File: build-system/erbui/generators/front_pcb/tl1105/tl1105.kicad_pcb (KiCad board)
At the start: 2 copper layers, 1 part, among them SW1 SW_Push_Dual

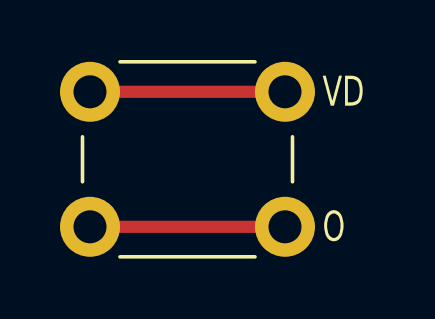
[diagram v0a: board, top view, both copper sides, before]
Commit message: Update erbui front pcb generator blocks labels to match boards conventions
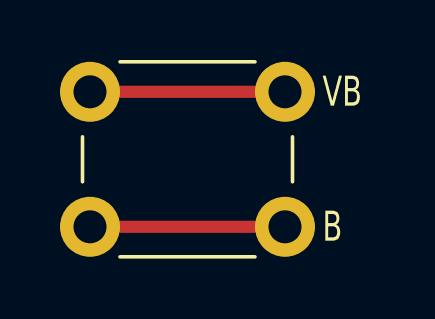
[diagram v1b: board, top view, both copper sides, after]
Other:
- board text added: "B"
- board text added: "VB"
- board text removed: "O"
- board text removed: "VD"
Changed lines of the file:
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@@
   )
   (setup
-    (last_trace_width 0.4064)
+    (last_trace_width 0.1524)
     (user_trace_width 0.1524)
     (user_trace_width 0.254)
@@
       (effects (font (size 1 1) (thickness 0.15)))
     )
+    (fp_line (start 3.25 -0.75) (end 6.25 -0.75) (layer F.Fab) (width 0.1))
+    (fp_line (start 6.25 -0.75) (end 6.25 5.25) (layer F.Fab) (width 0.1))
+    (fp_line (start 6.25 5.25) (end 0.25 5.25) (layer F.Fab) (width 0.1))
+    (fp_line (start 0.25 5.25) (end 0.25 -0.75) (layer F.Fab) (width 0.1))
+    (fp_line (start 0.25 -0.75) (end 3.25 -0.75) (layer F.Fab) (width 0.1))
+    (fp_line (start 7.75 6) (end 8 6) (layer F.CrtYd) (width 0.05))
+    (fp_line (start 8 6) (end 8 5.75) (layer F.CrtYd) (width 0.05))
+    (fp_line (start 7.75 -1.5) (end 8 -1.5) (layer F.CrtYd) (width 0.05))
+    (fp_line (start 8 -1.5) (end 8 -1.25) (layer F.CrtYd) (width 0.05))
+    (fp_line (start -1.5 -1.25) (end -1.5 -1.5) (layer F.CrtYd) (width 0.05))
+    (fp_line (start -1.5 -1.5) (end -1.25 -1.5) (layer F.CrtYd) (width 0.05))
+    (fp_line (start -1.5 5.75) (end -1.5 6) (layer F.CrtYd) (width 0.05))
+    (fp_line (start -1.5 6) (end -1.25 6) (layer F.CrtYd) (width 0.05))
+    (fp_line (start -1.25 -1.5) (end 7.75 -1.5) (layer F.CrtYd) (width 0.05))
+    (fp_line (start -1.5 5.75) (end -1.5 -1.25) (layer F.CrtYd) (width 0.05))
+    (fp_line (start 7.75 6) (end -1.25 6) (layer F.CrtYd) (width 0.05))
+    (fp_line (start 8 -1.25) (end 8 5.75) (layer F.CrtYd) (width 0.05))
+    (fp_line (start 1 5.5) (end 5.5 5.5) (layer F.SilkS) (width 0.12))
+    (fp_line (start -0.25 1.5) (end -0.25 3) (layer F.SilkS) (width 0.12))
+    (fp_line (start 5.5 -1) (end 1 -1) (layer F.SilkS) (width 0.12))
+    (fp_line (start 6.75 3) (end 6.75 1.5) (layer F.SilkS) (width 0.12))
     (fp_circle (center 3.25 2.25) (end 1.25 2.5) (layer F.Fab) (width 0.1))
-    (fp_line (start 6.75 3) (end 6.75 1.5) (layer F.SilkS) (width 0.12))
-    (fp_line (start 5.5 -1) (end 1 -1) (layer F.SilkS) (width 0.12))
-    (fp_line (start -0.25 1.5) (end -0.25 3) (layer F.SilkS) (width 0.12))
-    (fp_line (start 1 5.5) (end 5.5 5.5) (layer F.SilkS) (width 0.12))
-    (fp_line (start 8 -1.25) (end 8 5.75) (layer F.CrtYd) (width 0.05))
-    (fp_line (start 7.75 6) (end -1.25 6) (layer F.CrtYd) (width 0.05))
-    (fp_line (start -1.5 5.75) (end -1.5 -1.25) (layer F.CrtYd) (width 0.05))
-    (fp_line (start -1.25 -1.5) (end 7.75 -1.5) (layer F.CrtYd) (width 0.05))
-    (fp_line (start -1.5 6) (end -1.25 6) (layer F.CrtYd) (width 0.05))
-    (fp_line (start -1.5 5.75) (end -1.5 6) (layer F.CrtYd) (width 0.05))
-    (fp_line (start -1.5 -1.5) (end -1.25 -1.5) (layer F.CrtYd) (width 0.05))
-    (fp_line (start -1.5 -1.25) (end -1.5 -1.5) (layer F.CrtYd) (width 0.05))
-    (fp_line (start 8 -1.5) (end 8 -1.25) (layer F.CrtYd) (width 0.05))
-    (fp_line (start 7.75 -1.5) (end 8 -1.5) (layer F.CrtYd) (width 0.05))
-    (fp_line (start 8 6) (end 8 5.75) (layer F.CrtYd) (width 0.05))
-    (fp_line (start 7.75 6) (end 8 6) (layer F.CrtYd) (width 0.05))
-    (fp_line (start 0.25 -0.75) (end 3.25 -0.75) (layer F.Fab) (width 0.1))
-    (fp_line (start 0.25 5.25) (end 0.25 -0.75) (layer F.Fab) (width 0.1))
-    (fp_line (start 6.25 5.25) (end 0.25 5.25) (layer F.Fab) (width 0.1))
-    (fp_line (start 6.25 -0.75) (end 6.25 5.25) (layer F.Fab) (width 0.1))
-    (fp_line (start 3.25 -0.75) (end 6.25 -0.75) (layer F.Fab) (width 0.1))
     (fp_text user %R (at 3.25 2.25) (layer F.Fab)
       (effects (font (size 1 1) (thickness 0.15)))
@@
     )
   )
-  (gr_text O (at 4.5 2.25) (layer F.SilkS)
+  (gr_text B (at 4.5 2.25) (layer F.SilkS)
     (effects (font (size 1 0.7) (thickness 0.15)) (justify left))
   )
-  (gr_text VD (at 4.5 -2.25) (layer F.SilkS)
+  (gr_text VB (at 4.5 -2.25) (layer F.SilkS)
     (effects (font (size 1 0.7) (thickness 0.15)) (justify left))
   )

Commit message: Use pads to ease soldering
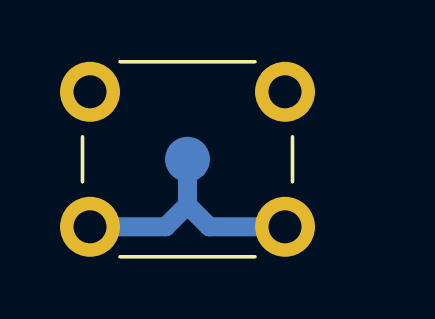
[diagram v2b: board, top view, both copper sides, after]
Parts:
- added TP1: TestPoint, TestPoint:TestPoint_Pad_D1.5mm, B.Cu at (0.00, 0.00)
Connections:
- net Net-(SW1-Pad1) renamed +3V3
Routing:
- net +3V3: track 6.50 -> 0.00 mm
- net Net-(SW1-Pad2): track 6.50 -> 8.63 mm
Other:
- board text added: "O"
- board text removed: "B"
- board text removed: "VB"
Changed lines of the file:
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@@
   (general
     (thickness 1.6)
-    (drawings 2)
-    (tracks 2)
+    (drawings 1)
+    (tracks 6)
     (zones 0)
-    (modules 1)
+    (modules 2)
     (nets 3)
   )
@@
   )
   (setup
-    (last_trace_width 0.1524)
+    (last_trace_width 0.635)
     (user_trace_width 0.1524)
     (user_trace_width 0.254)
@@
   (net 0 "")
   (net 1 "Net-(SW1-Pad2)")
-  (net 2 "Net-(SW1-Pad1)")
+  (net 2 +3V3)
   (net_class Default "This is the default net class."
     (clearance 0.1524)
@@
     (diff_pair_width 0.1524)
     (diff_pair_gap 0.1524)
-    (add_net "Net-(SW1-Pad1)")
+    (add_net +3V3)
     (add_net "Net-(SW1-Pad2)")
   )
@@
       (effects (font (size 1 1) (thickness 0.15)))
     )
+    (fp_circle (center 3.25 2.25) (end 1.25 2.5) (layer F.Fab) (width 0.1))
+    (fp_line (start 6.75 3) (end 6.75 1.5) (layer F.SilkS) (width 0.12))
+    (fp_line (start 5.5 -1) (end 1 -1) (layer F.SilkS) (width 0.12))
+    (fp_line (start -0.25 1.5) (end -0.25 3) (layer F.SilkS) (width 0.12))
+    (fp_line (start 1 5.5) (end 5.5 5.5) (layer F.SilkS) (width 0.12))
+    (fp_line (start 8 -1.25) (end 8 5.75) (layer F.CrtYd) (width 0.05))
+    (fp_line (start 7.75 6) (end -1.25 6) (layer F.CrtYd) (width 0.05))
+    (fp_line (start -1.5 5.75) (end -1.5 -1.25) (layer F.CrtYd) (width 0.05))
+    (fp_line (start -1.25 -1.5) (end 7.75 -1.5) (layer F.CrtYd) (width 0.05))
+    (fp_line (start -1.5 6) (end -1.25 6) (layer F.CrtYd) (width 0.05))
+    (fp_line (start -1.5 5.75) (end -1.5 6) (layer F.CrtYd) (width 0.05))
+    (fp_line (start -1.5 -1.5) (end -1.25 -1.5) (layer F.CrtYd) (width 0.05))
+    (fp_line (start -1.5 -1.25) (end -1.5 -1.5) (layer F.CrtYd) (width 0.05))
+    (fp_line (start 8 -1.5) (end 8 -1.25) (layer F.CrtYd) (width 0.05))
+    (fp_line (start 7.75 -1.5) (end 8 -1.5) (layer F.CrtYd) (width 0.05))
+    (fp_line (start 8 6) (end 8 5.75) (layer F.CrtYd) (width 0.05))
+    (fp_line (start 7.75 6) (end 8 6) (layer F.CrtYd) (width 0.05))
+    (fp_line (start 0.25 -0.75) (end 3.25 -0.75) (layer F.Fab) (width 0.1))
+    (fp_line (start 0.25 5.25) (end 0.25 -0.75) (layer F.Fab) (width 0.1))
+    (fp_line (start 6.25 5.25) (end 0.25 5.25) (layer F.Fab) (width 0.1))
+    (fp_line (start 6.25 -0.75) (end 6.25 5.25) (layer F.Fab) (width 0.1))
     (fp_line (start 3.25 -0.75) (end 6.25 -0.75) (layer F.Fab) (width 0.1))
-    (fp_line (start 6.25 -0.75) (end 6.25 5.25) (layer F.Fab) (width 0.1))
-    (fp_line (start 6.25 5.25) (end 0.25 5.25) (layer F.Fab) (width 0.1))
-    (fp_line (start 0.25 5.25) (end 0.25 -0.75) (layer F.Fab) (width 0.1))
-    (fp_line (start 0.25 -0.75) (end 3.25 -0.75) (layer F.Fab) (width 0.1))
-    (fp_line (start 7.75 6) (end 8 6) (layer F.CrtYd) (width 0.05))
-    (fp_line (start 8 6) (end 8 5.75) (layer F.CrtYd) (width 0.05))
-    (fp_line (start 7.75 -1.5) (end 8 -1.5) (layer F.CrtYd) (width 0.05))
-    (fp_line (start 8 -1.5) (end 8 -1.25) (layer F.CrtYd) (width 0.05))
-    (fp_line (start -1.5 -1.25) (end -1.5 -1.5) (layer F.CrtYd) (width 0.05))
-    (fp_line (start -1.5 -1.5) (end -1.25 -1.5) (layer F.CrtYd) (width 0.05))
-    (fp_line (start -1.5 5.75) (end -1.5 6) (layer F.CrtYd) (width 0.05))
-    (fp_line (start -1.5 6) (end -1.25 6) (layer F.CrtYd) (width 0.05))
-    (fp_line (start -1.25 -1.5) (end 7.75 -1.5) (layer F.CrtYd) (width 0.05))
-    (fp_line (start -1.5 5.75) (end -1.5 -1.25) (layer F.CrtYd) (width 0.05))
-    (fp_line (start 7.75 6) (end -1.25 6) (layer F.CrtYd) (width 0.05))
-    (fp_line (start 8 -1.25) (end 8 5.75) (layer F.CrtYd) (width 0.05))
-    (fp_line (start 1 5.5) (end 5.5 5.5) (layer F.SilkS) (width 0.12))
-    (fp_line (start -0.25 1.5) (end -0.25 3) (layer F.SilkS) (width 0.12))
-    (fp_line (start 5.5 -1) (end 1 -1) (layer F.SilkS) (width 0.12))
-    (fp_line (start 6.75 3) (end 6.75 1.5) (layer F.SilkS) (width 0.12))
-    (fp_circle (center 3.25 2.25) (end 1.25 2.5) (layer F.Fab) (width 0.1))
     (fp_text user %R (at 3.25 2.25) (layer F.Fab)
       (effects (font (size 1 1) (thickness 0.15)))
@@
       (net 1 "Net-(SW1-Pad2)"))
     (pad 1 thru_hole circle (at 0 0 90) (size 2 2) (drill 1.1) (layers *.Cu *.Mask)
-      (net 2 "Net-(SW1-Pad1)"))
+      (net 2 +3V3))
     (pad 2 thru_hole circle (at 6.5 4.5 90) (size 2 2) (drill 1.1) (layers *.Cu *.Mask)
       (net 1 "Net-(SW1-Pad2)"))
     (pad 1 thru_hole circle (at 6.5 0 90) (size 2 2) (drill 1.1) (layers *.Cu *.Mask)
-      (net 2 "Net-(SW1-Pad1)"))
+      (net 2 +3V3))
     (model ${KISYS3DMOD}/Button_Switch_THT.3dshapes/SW_PUSH_6mm_H7.3mm.wrl
       (at (xyz 0 0 0))
@@
     )
   )
-  (gr_text B (at 4.5 2.25) (layer F.SilkS)
-    (effects (font (size 1 0.7) (thickness 0.15)) (justify left))
+  (module TestPoint:TestPoint_Pad_D1.5mm (layer B.Cu)
+    (at 0 0)
+    (descr "SMD pad as test Point, diameter 1.5mm")
+    (tags "test point SMD pad")
+    (attr virtual)
+    (fp_text reference TP1 (at 0 1.648) (layer B.SilkS) hide
+      (effects (font (size 1 1) (thickness 0.15)) (justify mirror))
+    )
+    (fp_text value TestPoint (at 0 -1.75) (layer B.Fab)
+      (effects (font (size 1 1) (thickness 0.15)) (justify mirror))
+    )
+    (fp_circle (center 0 0) (end 0 -0.95) (layer B.SilkS) (width 0.12))
+    (fp_circle (center 0 0) (end 1.25 0) (layer B.CrtYd) (width 0.05))
+    (fp_text user %R (at 0 1.65) (layer B.Fab)
+      (effects (font (size 1 1) (thickness 0.15)) (justify mirror))
+    )
+    (pad 1 smd circle (at 0 0) (size 1.5 1.5) (layers B.Cu B.Mask)
+      (net 1 "Net-(SW1-Pad2)"))
   )
-  (gr_text VB (at 4.5 -2.25) (layer F.SilkS)
-    (effects (font (size 1 0.7) (thickness 0.15)) (justify left))
+  (gr_text O (at 2.159 0) (layer B.SilkS)
+    (effects (font (size 1 1) (thickness 0.15)) (justify left mirror))
   )
-  (segment (start -3.25 2.25) (end 3.25 2.25) (width 0.4064) (layer F.Cu) (net 1))
-  (segment (start -3.25 -2.25) (end 3.25 -2.25) (width 0.4064) (layer F.Cu) (net 2))
+  (segment (start 0 1.016) (end 0 0) (width 0.635) (layer B.Cu) (net 1))
+  (segment (start 0 1.524) (end 0 1.016) (width 0.635) (layer B.Cu) (net 1))
+  (segment (start -0.726 2.25) (end 0 1.524) (width 0.635) (layer B.Cu) (net 1))
+  (segment (start -3.25 2.25) (end -0.726 2.25) (width 0.635) (layer B.Cu) (net 1))
+  (segment (start 0.726 2.25) (end 0 1.524) (width 0.635) (layer B.Cu) (net 1))
+  (segment (start 3.25 2.25) (end 0.726 2.25) (width 0.635) (layer B.Cu) (net 1))
 )

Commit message: Generate pin associations
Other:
- board text added: "pin"
- board text removed: "O"
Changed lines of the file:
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@@
   )
   (setup
-    (last_trace_width 0.635)
+    (last_trace_width 0.1524)
     (user_trace_width 0.1524)
     (user_trace_width 0.254)
@@
       (effects (font (size 1 1) (thickness 0.15)))
     )
+    (fp_line (start 3.25 -0.75) (end 6.25 -0.75) (layer F.Fab) (width 0.1))
+    (fp_line (start 6.25 -0.75) (end 6.25 5.25) (layer F.Fab) (width 0.1))
+    (fp_line (start 6.25 5.25) (end 0.25 5.25) (layer F.Fab) (width 0.1))
+    (fp_line (start 0.25 5.25) (end 0.25 -0.75) (layer F.Fab) (width 0.1))
+    (fp_line (start 0.25 -0.75) (end 3.25 -0.75) (layer F.Fab) (width 0.1))
+    (fp_line (start 7.75 6) (end 8 6) (layer F.CrtYd) (width 0.05))
+    (fp_line (start 8 6) (end 8 5.75) (layer F.CrtYd) (width 0.05))
+    (fp_line (start 7.75 -1.5) (end 8 -1.5) (layer F.CrtYd) (width 0.05))
+    (fp_line (start 8 -1.5) (end 8 -1.25) (layer F.CrtYd) (width 0.05))
+    (fp_line (start -1.5 -1.25) (end -1.5 -1.5) (layer F.CrtYd) (width 0.05))
+    (fp_line (start -1.5 -1.5) (end -1.25 -1.5) (layer F.CrtYd) (width 0.05))
+    (fp_line (start -1.5 5.75) (end -1.5 6) (layer F.CrtYd) (width 0.05))
+    (fp_line (start -1.5 6) (end -1.25 6) (layer F.CrtYd) (width 0.05))
+    (fp_line (start -1.25 -1.5) (end 7.75 -1.5) (layer F.CrtYd) (width 0.05))
+    (fp_line (start -1.5 5.75) (end -1.5 -1.25) (layer F.CrtYd) (width 0.05))
+    (fp_line (start 7.75 6) (end -1.25 6) (layer F.CrtYd) (width 0.05))
+    (fp_line (start 8 -1.25) (end 8 5.75) (layer F.CrtYd) (width 0.05))
+    (fp_line (start 1 5.5) (end 5.5 5.5) (layer F.SilkS) (width 0.12))
+    (fp_line (start -0.25 1.5) (end -0.25 3) (layer F.SilkS) (width 0.12))
+    (fp_line (start 5.5 -1) (end 1 -1) (layer F.SilkS) (width 0.12))
+    (fp_line (start 6.75 3) (end 6.75 1.5) (layer F.SilkS) (width 0.12))
     (fp_circle (center 3.25 2.25) (end 1.25 2.5) (layer F.Fab) (width 0.1))
-    (fp_line (start 6.75 3) (end 6.75 1.5) (layer F.SilkS) (width 0.12))
-    (fp_line (start 5.5 -1) (end 1 -1) (layer F.SilkS) (width 0.12))
-    (fp_line (start -0.25 1.5) (end -0.25 3) (layer F.SilkS) (width 0.12))
-    (fp_line (start 1 5.5) (end 5.5 5.5) (layer F.SilkS) (width 0.12))
-    (fp_line (start 8 -1.25) (end 8 5.75) (layer F.CrtYd) (width 0.05))
-    (fp_line (start 7.75 6) (end -1.25 6) (layer F.CrtYd) (width 0.05))
-    (fp_line (start -1.5 5.75) (end -1.5 -1.25) (layer F.CrtYd) (width 0.05))
-    (fp_line (start -1.25 -1.5) (end 7.75 -1.5) (layer F.CrtYd) (width 0.05))
-    (fp_line (start -1.5 6) (end -1.25 6) (layer F.CrtYd) (width 0.05))
-    (fp_line (start -1.5 5.75) (end -1.5 6) (layer F.CrtYd) (width 0.05))
-    (fp_line (start -1.5 -1.5) (end -1.25 -1.5) (layer F.CrtYd) (width 0.05))
-    (fp_line (start -1.5 -1.25) (end -1.5 -1.5) (layer F.CrtYd) (width 0.05))
-    (fp_line (start 8 -1.5) (end 8 -1.25) (layer F.CrtYd) (width 0.05))
-    (fp_line (start 7.75 -1.5) (end 8 -1.5) (layer F.CrtYd) (width 0.05))
-    (fp_line (start 8 6) (end 8 5.75) (layer F.CrtYd) (width 0.05))
-    (fp_line (start 7.75 6) (end 8 6) (layer F.CrtYd) (width 0.05))
-    (fp_line (start 0.25 -0.75) (end 3.25 -0.75) (layer F.Fab) (width 0.1))
-    (fp_line (start 0.25 5.25) (end 0.25 -0.75) (layer F.Fab) (width 0.1))
-    (fp_line (start 6.25 5.25) (end 0.25 5.25) (layer F.Fab) (width 0.1))
-    (fp_line (start 6.25 -0.75) (end 6.25 5.25) (layer F.Fab) (width 0.1))
-    (fp_line (start 3.25 -0.75) (end 6.25 -0.75) (layer F.Fab) (width 0.1))
     (fp_text user %R (at 3.25 2.25) (layer F.Fab)
       (effects (font (size 1 1) (thickness 0.15)))
@@
       (effects (font (size 1 1) (thickness 0.15)) (justify mirror))
     )
+    (fp_circle (center 0 0) (end 1.25 0) (layer B.CrtYd) (width 0.05))
     (fp_circle (center 0 0) (end 0 -0.95) (layer B.SilkS) (width 0.12))
-    (fp_circle (center 0 0) (end 1.25 0) (layer B.CrtYd) (width 0.05))
     (fp_text user %R (at 0 1.65) (layer B.Fab)
       (effects (font (size 1 1) (thickness 0.15)) (justify mirror))
@@
       (net 1 "Net-(SW1-Pad2)"))
   )
-  (gr_text O (at 2.159 0) (layer B.SilkS)
-    (effects (font (size 1 1) (thickness 0.15)) (justify left mirror))
+  (gr_text pin (at 1.016 0) (layer B.SilkS)
+    (effects (font (size 1 1) (thickness 0.15)) (justify right mirror))
   )
   (segment (start 0 1.016) (end 0 0) (width 0.635) (layer B.Cu) (net 1))

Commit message: Assign predictable pin names to controls
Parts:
- renumbered TP1 to Pin0, SW1 to ZZ1
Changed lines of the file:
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@@
   )
   (net 0 "")
-  (net 1 "Net-(SW1-Pad2)")
-  (net 2 +3V3)
+  (net 1 +3V3)
+  (net 2 "Net-(Pin0-Pad1)")
   (net_class Default "This is the default net class."
     (clearance 0.1524)
@@
     (diff_pair_gap 0.1524)
     (add_net +3V3)
-    (add_net "Net-(SW1-Pad2)")
+    (add_net "Net-(Pin0-Pad1)")
   )
   (module Button_Switch_THT:SW_PUSH_6mm_H7.3mm (layer F.Cu)
@@
     (descr "tactile push button, 6x6mm e.g. PHAP33xx series, height=7.3mm")
     (tags "tact sw push 6mm")
-    (fp_text reference SW1 (at 3.25 -2) (layer F.SilkS) hide
+    (fp_text reference ZZ1 (at 3.25 -2) (layer F.SilkS) hide
       (effects (font (size 1 1) (thickness 0.15)))
     )
@@
       (effects (font (size 1 1) (thickness 0.15)))
     )
+    (fp_circle (center 3.25 2.25) (end 1.25 2.5) (layer F.Fab) (width 0.1))
+    (fp_line (start 6.75 3) (end 6.75 1.5) (layer F.SilkS) (width 0.12))
+    (fp_line (start 5.5 -1) (end 1 -1) (layer F.SilkS) (width 0.12))
+    (fp_line (start -0.25 1.5) (end -0.25 3) (layer F.SilkS) (width 0.12))
+    (fp_line (start 1 5.5) (end 5.5 5.5) (layer F.SilkS) (width 0.12))
+    (fp_line (start 8 -1.25) (end 8 5.75) (layer F.CrtYd) (width 0.05))
+    (fp_line (start 7.75 6) (end -1.25 6) (layer F.CrtYd) (width 0.05))
+    (fp_line (start -1.5 5.75) (end -1.5 -1.25) (layer F.CrtYd) (width 0.05))
+    (fp_line (start -1.25 -1.5) (end 7.75 -1.5) (layer F.CrtYd) (width 0.05))
+    (fp_line (start -1.5 6) (end -1.25 6) (layer F.CrtYd) (width 0.05))
+    (fp_line (start -1.5 5.75) (end -1.5 6) (layer F.CrtYd) (width 0.05))
+    (fp_line (start -1.5 -1.5) (end -1.25 -1.5) (layer F.CrtYd) (width 0.05))
+    (fp_line (start -1.5 -1.25) (end -1.5 -1.5) (layer F.CrtYd) (width 0.05))
+    (fp_line (start 8 -1.5) (end 8 -1.25) (layer F.CrtYd) (width 0.05))
+    (fp_line (start 7.75 -1.5) (end 8 -1.5) (layer F.CrtYd) (width 0.05))
+    (fp_line (start 8 6) (end 8 5.75) (layer F.CrtYd) (width 0.05))
+    (fp_line (start 7.75 6) (end 8 6) (layer F.CrtYd) (width 0.05))
+    (fp_line (start 0.25 -0.75) (end 3.25 -0.75) (layer F.Fab) (width 0.1))
+    (fp_line (start 0.25 5.25) (end 0.25 -0.75) (layer F.Fab) (width 0.1))
+    (fp_line (start 6.25 5.25) (end 0.25 5.25) (layer F.Fab) (width 0.1))
+    (fp_line (start 6.25 -0.75) (end 6.25 5.25) (layer F.Fab) (width 0.1))
     (fp_line (start 3.25 -0.75) (end 6.25 -0.75) (layer F.Fab) (width 0.1))
-    (fp_line (start 6.25 -0.75) (end 6.25 5.25) (layer F.Fab) (width 0.1))
-    (fp_line (start 6.25 5.25) (end 0.25 5.25) (layer F.Fab) (width 0.1))
-    (fp_line (start 0.25 5.25) (end 0.25 -0.75) (layer F.Fab) (width 0.1))
-    (fp_line (start 0.25 -0.75) (end 3.25 -0.75) (layer F.Fab) (width 0.1))
-    (fp_line (start 7.75 6) (end 8 6) (layer F.CrtYd) (width 0.05))
-    (fp_line (start 8 6) (end 8 5.75) (layer F.CrtYd) (width 0.05))
-    (fp_line (start 7.75 -1.5) (end 8 -1.5) (layer F.CrtYd) (width 0.05))
-    (fp_line (start 8 -1.5) (end 8 -1.25) (layer F.CrtYd) (width 0.05))
-    (fp_line (start -1.5 -1.25) (end -1.5 -1.5) (layer F.CrtYd) (width 0.05))
-    (fp_line (start -1.5 -1.5) (end -1.25 -1.5) (layer F.CrtYd) (width 0.05))
-    (fp_line (start -1.5 5.75) (end -1.5 6) (layer F.CrtYd) (width 0.05))
-    (fp_line (start -1.5 6) (end -1.25 6) (layer F.CrtYd) (width 0.05))
-    (fp_line (start -1.25 -1.5) (end 7.75 -1.5) (layer F.CrtYd) (width 0.05))
-    (fp_line (start -1.5 5.75) (end -1.5 -1.25) (layer F.CrtYd) (width 0.05))
-    (fp_line (start 7.75 6) (end -1.25 6) (layer F.CrtYd) (width 0.05))
-    (fp_line (start 8 -1.25) (end 8 5.75) (layer F.CrtYd) (width 0.05))
-    (fp_line (start 1 5.5) (end 5.5 5.5) (layer F.SilkS) (width 0.12))
-    (fp_line (start -0.25 1.5) (end -0.25 3) (layer F.SilkS) (width 0.12))
-    (fp_line (start 5.5 -1) (end 1 -1) (layer F.SilkS) (width 0.12))
-    (fp_line (start 6.75 3) (end 6.75 1.5) (layer F.SilkS) (width 0.12))
-    (fp_circle (center 3.25 2.25) (end 1.25 2.5) (layer F.Fab) (width 0.1))
     (fp_text user %R (at 3.25 2.25) (layer F.Fab)
       (effects (font (size 1 1) (thickness 0.15)))
     )
     (pad 2 thru_hole circle (at 0 4.5 90) (size 2 2) (drill 1.1) (layers *.Cu *.Mask)
-      (net 1 "Net-(SW1-Pad2)"))
+      (net 2 "Net-(Pin0-Pad1)"))
     (pad 1 thru_hole circle (at 0 0 90) (size 2 2) (drill 1.1) (layers *.Cu *.Mask)
-      (net 2 +3V3))
+      (net 1 +3V3))
     (pad 2 thru_hole circle (at 6.5 4.5 90) (size 2 2) (drill 1.1) (layers *.Cu *.Mask)
-      (net 1 "Net-(SW1-Pad2)"))
+      (net 2 "Net-(Pin0-Pad1)"))
     (pad 1 thru_hole circle (at 6.5 0 90) (size 2 2) (drill 1.1) (layers *.Cu *.Mask)
-      (net 2 +3V3))
+      (net 1 +3V3))
     (model ${KISYS3DMOD}/Button_Switch_THT.3dshapes/SW_PUSH_6mm_H7.3mm.wrl
       (at (xyz 0 0 0))
@@
     (tags "test point SMD pad")
     (attr virtual)
-    (fp_text reference TP1 (at 0 1.648) (layer B.SilkS) hide
+    (fp_text reference Pin0 (at 0 1.648) (layer B.SilkS) hide
       (effects (font (size 1 1) (thickness 0.15)) (justify mirror))
     )
@@
       (effects (font (size 1 1) (thickness 0.15)) (justify mirror))
     )
+    (fp_circle (center 0 0) (end 0 -0.95) (layer B.SilkS) (width 0.12))
     (fp_circle (center 0 0) (end 1.25 0) (layer B.CrtYd) (width 0.05))
-    (fp_circle (center 0 0) (end 0 -0.95) (layer B.SilkS) (width 0.12))
     (fp_text user %R (at 0 1.65) (layer B.Fab)
       (effects (font (size 1 1) (thickness 0.15)) (justify mirror))
     )
     (pad 1 smd circle (at 0 0) (size 1.5 1.5) (layers B.Cu B.Mask)
-      (net 1 "Net-(SW1-Pad2)"))
+      (net 2 "Net-(Pin0-Pad1)"))
   )
   (gr_text pin (at 1.016 0) (layer B.SilkS)
     (effects (font (size 1 1) (thickness 0.15)) (justify right mirror))
   )
-  (segment (start 0 1.016) (end 0 0) (width 0.635) (layer B.Cu) (net 1))
-  (segment (start 0 1.524) (end 0 1.016) (width 0.635) (layer B.Cu) (net 1))
-  (segment (start -0.726 2.25) (end 0 1.524) (width 0.635) (layer B.Cu) (net 1))
-  (segment (start -3.25 2.25) (end -0.726 2.25) (width 0.635) (layer B.Cu) (net 1))
-  (segment (start 0.726 2.25) (end 0 1.524) (width 0.635) (layer B.Cu) (net 1))
-  (segment (start 3.25 2.25) (end 0.726 2.25) (width 0.635) (layer B.Cu) (net 1))
+  (segment (start 0 1.016) (end 0 0) (width 0.635) (layer B.Cu) (net 2))
+  (segment (start 0 1.524) (end 0 1.016) (width 0.635) (layer B.Cu) (net 2))
+  (segment (start -0.726 2.25) (end 0 1.524) (width 0.635) (layer B.Cu) (net 2))
+  (segment (start -3.25 2.25) (end -0.726 2.25) (width 0.635) (layer B.Cu) (net 2))
+  (segment (start 0.726 2.25) (end 0 1.524) (width 0.635) (layer B.Cu) (net 2))
+  (segment (start 3.25 2.25) (end 0.726 2.25) (width 0.635) (layer B.Cu) (net 2))
 )
